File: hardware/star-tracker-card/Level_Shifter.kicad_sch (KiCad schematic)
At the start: 48 parts, among them U5 SN74LVC8T245MPWREPPW24-M, U6 CLVCH16T245MDGGREP, U8 TLV70028QDDCRQ1, U9 TCA9509DGKRDGK8-M

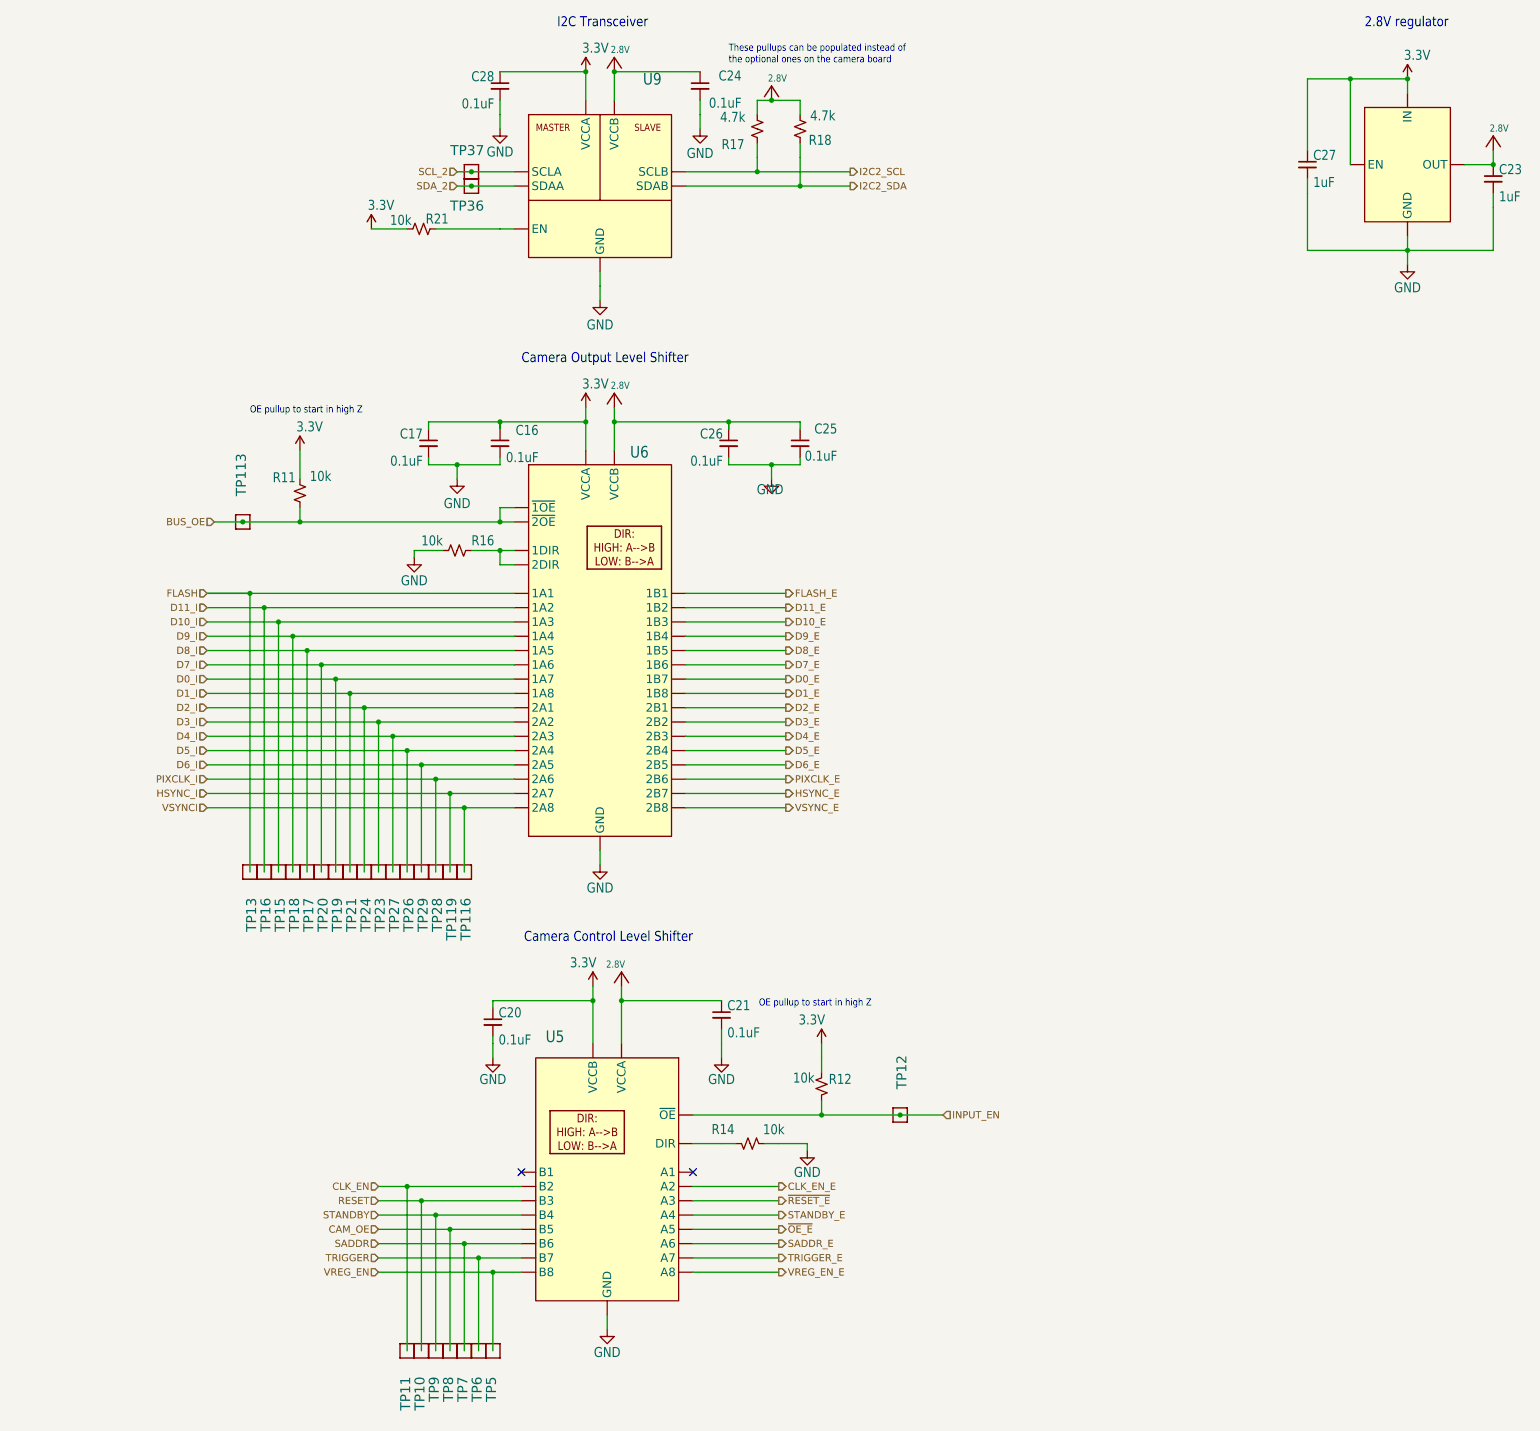
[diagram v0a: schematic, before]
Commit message: Big almost-done cleanup
Fixed a bunch of things in the schematic. Compared against C3 Octavo. Fixed all weird ERCs. Cleaned up a lot of planes on the layout. Moved uart switch, rerouted a bunch of traces for better layout. Fixed library issues, and board/sch sync issues.
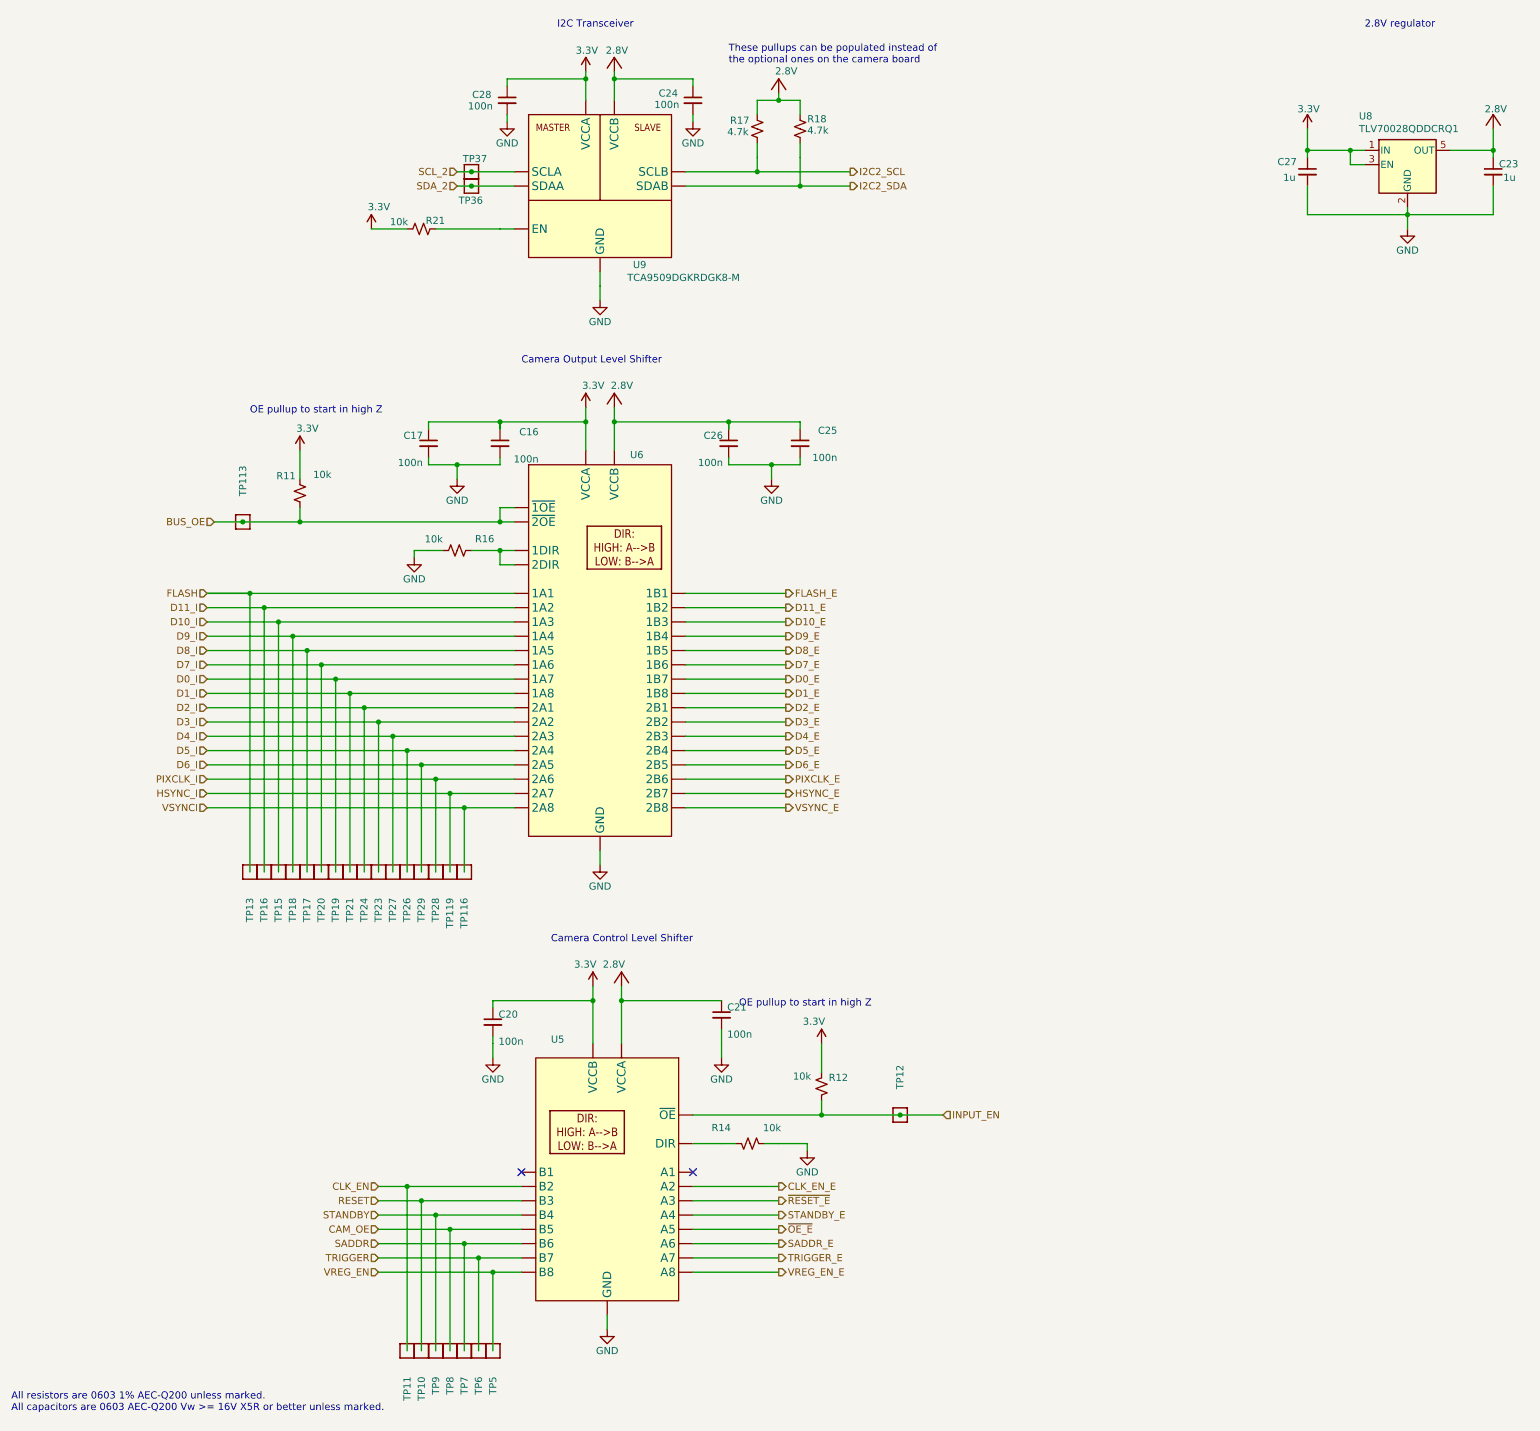
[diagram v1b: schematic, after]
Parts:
- C16, C17, C20, C21, C24, C25, C26, C28: value 0.1uF -> 100n; footprint oresat-passives:c_0603-SMALL -> oresat-passives:0603-C-NOSILK
- C23, C27: value 1uF -> 1u; footprint oresat-passives:c_0603-SMALL -> oresat-passives:0603-C-NOSILK
- R11, R12, R14, R16, R17, R18, R21: footprint Resistor_SMD:R_0603_1608Metric -> oresat-passives:0603-C-NOSILK
- U8: footprint star-tracker-card:SOT23-5 -> Package_TO_SOT_SMD:SOT-23-5; symbol star-tracker-card-eagle-import:TLV70028QDDCRQ1 -> Regulator_Linear:TLV70028_SOT353
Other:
- note added: "All resistors are 0603 1% AEC-Q200 unless marked. All capacitors are 0603 AEC-Q200 Vw >= 16V X5R or better unless marked."
- company: (none) -> Portland State Aerospace Society
- title: (none) -> OreSat Star Tracker
- moved on the sheet: C23, C24, C27, C28

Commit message: BOM 99% completed, push for final review
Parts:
- C16, C17, C20, C21, C24, C25, C26, C28: DIS (none) -> DigiKey; DPN (none) -> 399-6856-1-ND; MFR (none) -> KEMET; MPN (none) -> C0603C104K5RACAUTO
- C23, C27: DIS (none) -> DigiKey; DPN (none) -> 490-GRT188R71E105KE13DCT-ND; MFR (none) -> Murata Electronics; MPN (none) -> GRT188R71E105KE13D
- R11, R12, R14, R16, R21: DIS (none) -> DigiKey; DPN (none) -> RMCF0603FT10K0CT-ND; MFR (none) -> Stackpole Electronics; MPN (none) -> RMCF0603FT10K0
- R17, R18: DIS (none) -> DigiKey; DPN (none) -> RMCF0603FT4K70CT-ND; MFR (none) -> Stackpole Electronics; MPN (none) -> RMCF0603FT4K70
- U5: DIS (none) -> DigiKey; DPN (none) -> 296-18593-1-ND; MFR (none) -> Texas Instruments; MPN (none) -> SN74LVC8T245PWR
- U6: DIS (none) -> DigiKey; DPN (none) -> 296-23948-1-ND; MFR (none) -> Texas Instruments; MPN (none) -> CLVCH16T245MDGGREP
- U9: DIS (none) -> DigiKey; DPN (none) -> 296-30283-1-ND; MFR (none) -> Texas Instruments; MPN (none) -> TCA9509DGKR

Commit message: Star Tracker v1.3 files, including new Makefile, Readme, and fixes in ERC, DRC, and layout
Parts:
- U8: DIS (none) -> Mouser; DPN (none) -> 595-TLV70028QDDCRQ1; MFR (none) -> Texas Instruments; MPN (none) -> TLV70028QDDCRQ1
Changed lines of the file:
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@@
 	(title_block
 		(title "OreSat Star Tracker")
-		(date "2026-04-15")
+		(date "2026-04-22")
 		(rev "1.3")
 		(company "Portland State Aerospace Society")
@@
 			(at 360.68 44.45 0)
 			(hide yes)
+			(show_name no)
+			(do_not_autoplace no)
+			(effects
+				(font
+					(size 1.27 1.27)
+				)
+			)
+		)
+		(property "DIS" "Mouser"
+			(at 360.68 44.45 0)
+			(hide yes)
+			(show_name no)
+			(do_not_autoplace no)
+			(effects
+				(font
+					(size 1.27 1.27)
+				)
+			)
+		)
+		(property "DPN" "595-TLV70028QDDCRQ1"
+			(at 360.68 44.45 0)
+			(hide yes)
+			(show_name no)
+			(do_not_autoplace no)
+			(effects
+				(font
+					(size 1.27 1.27)
+				)
+			)
+		)
+		(property "MFR" "Texas Instruments"
+			(at 360.68 44.45 0)
+			(hide yes)
+			(show_name no)
+			(do_not_autoplace no)
+			(effects
+				(font
+					(size 1.27 1.27)
+				)
+			)
+		)
+		(property "MPN" "TLV70028QDDCRQ1"
+			(at 360.68 44.45 0)
+			(hide yes)
